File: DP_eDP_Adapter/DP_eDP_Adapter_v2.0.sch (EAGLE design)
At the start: 61 parts, among them IC1 AP6502A, IC2 tiny2313, IC3 TLC5947XLP

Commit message: 
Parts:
- SV3: value DP_EDP_ADAPTER_EDP_CONNECTOR -> DP_EDP_ADAPTER_DP_EDP_ADAPTER_EDP_CONNECTOR; device DP_eDP_Adapter:DP_EDP_ADAPTER_EDP_CONNECTOR -> DP_eDP_Adapter_v2.0:DP_EDP_ADAPTER_DP_EDP_ADAPTER_EDP_CONNECTOR
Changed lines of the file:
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@@
 <part name="+3V3" library="supply1" deviceset="+3V3" device=""/>
 <part name="SIG_OUT" library="SparkFun-Connectors" deviceset="M04" device="PTH"/>
-<part name="SV3" library="DP_eDP_Adapter" deviceset="DP_EDP_ADAPTER_EDP_CONNECTOR" device=""/>
+<part name="SV3" library="DP_eDP_Adapter_v2.0" deviceset="DP_EDP_ADAPTER_DP_EDP_ADAPTER_EDP_CONNECTOR" device=""/>
 <part name="GND4" library="supply1" deviceset="GND" device=""/>
 <part name="JP3" library="SparkFun-Connectors" deviceset="M05" device="PTH"/>

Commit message: 
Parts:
- C17: device SparkFun-Passives:CAP0402-CAP -> SparkFun-Passives:CAP0805
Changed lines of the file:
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@@
 <grid distance="0.1" unitdist="inch" unit="inch" style="lines" multiple="1" display="no" altdistance="0.01" altunitdist="inch" altunit="inch"/>
 <layers>
-<layer number="1" name="Top" color="4" fill="1" visible="no" active="no"/>
-<layer number="2" name="Route2" color="1" fill="3" visible="no" active="no"/>
-<layer number="3" name="Route3" color="4" fill="3" visible="no" active="no"/>
-<layer number="4" name="Route4" color="1" fill="4" visible="no" active="no"/>
-<layer number="5" name="Route5" color="4" fill="4" visible="no" active="no"/>
-<layer number="6" name="Route6" color="1" fill="8" visible="no" active="no"/>
-<layer number="7" name="Route7" color="4" fill="8" visible="no" active="no"/>
-<layer number="8" name="Route8" color="1" fill="2" visible="no" active="no"/>
-<layer number="9" name="Route9" color="4" fill="2" visible="no" active="no"/>
-<layer number="10" name="Route10" color="1" fill="7" visible="no" active="no"/>
-<layer number="11" name="Route11" color="4" fill="7" visible="no" active="no"/>
-<layer number="12" name="Route12" color="1" fill="5" visible="no" active="no"/>
-<layer number="13" name="Route13" color="4" fill="5" visible="no" active="no"/>
-<layer number="14" name="Route14" color="1" fill="6" visible="no" active="no"/>
-<layer number="15" name="Route15" color="4" fill="6" visible="no" active="no"/>
-<layer number="16" name="Bottom" color="1" fill="1" visible="no" active="no"/>
-<layer number="17" name="Pads" color="2" fill="1" visible="no" active="no"/>
-<layer number="18" name="Vias" color="2" fill="1" visible="no" active="no"/>
-<layer number="19" name="Unrouted" color="6" fill="1" visible="no" active="no"/>
-<layer number="20" name="Dimension" color="15" fill="1" visible="no" active="no"/>
-<layer number="21" name="tPlace" color="7" fill="1" visible="no" active="no"/>
-<layer number="22" name="bPlace" color="7" fill="1" visible="no" active="no"/>
-<layer number="23" name="tOrigins" color="15" fill="1" visible="no" active="no"/>
-<layer number="24" name="bOrigins" color="15" fill="1" visible="no" active="no"/>
-<layer number="25" name="tNames" color="7" fill="1" visible="no" active="no"/>
-<layer number="26" name="bNames" color="7" fill="1" visible="no" active="no"/>
-<layer number="27" name="tValues" color="7" fill="1" visible="no" active="no"/>
-<layer number="28" name="bValues" color="7" fill="1" visible="no" active="no"/>
+<layer number="1" name="Top" color="4" fill="1" visible="yes" active="no"/>
+<layer number="2" name="Route2" color="1" fill="3" visible="yes" active="no"/>
+<layer number="3" name="Route3" color="4" fill="3" visible="yes" active="no"/>
+<layer number="4" name="Route4" color="1" fill="4" visible="yes" active="no"/>
+<layer number="5" name="Route5" color="4" fill="4" visible="yes" active="no"/>
+<layer number="6" name="Route6" color="1" fill="8" visible="yes" active="no"/>
+<layer number="7" name="Route7" color="4" fill="8" visible="yes" active="no"/>
+<layer number="8" name="Route8" color="1" fill="2" visible="yes" active="no"/>
+<layer number="9" name="Route9" color="4" fill="2" visible="yes" active="no"/>
+<layer number="10" name="Route10" color="1" fill="7" visible="yes" active="no"/>
+<layer number="11" name="Route11" color="4" fill="7" visible="yes" active="no"/>
+<layer number="12" name="Route12" color="1" fill="5" visible="yes" active="no"/>
+<layer number="13" name="Route13" color="4" fill="5" visible="yes" active="no"/>
+<layer number="14" name="Route14" color="1" fill="6" visible="yes" active="no"/>
+<layer number="15" name="Route15" color="4" fill="6" visible="yes" active="no"/>
+<layer number="16" name="Bottom" color="1" fill="1" visible="yes" active="no"/>
+<layer number="17" name="Pads" color="2" fill="1" visible="yes" active="no"/>
+<layer number="18" name="Vias" color="2" fill="1" visible="yes" active="no"/>
+<layer number="19" name="Unrouted" color="6" fill="1" visible="yes" active="no"/>
+<layer number="20" name="Dimension" color="15" fill="1" visible="yes" active="no"/>
+<layer number="21" name="tPlace" color="7" fill="1" visible="yes" active="no"/>
+<layer number="22" name="bPlace" color="7" fill="1" visible="yes" active="no"/>
+<layer number="23" name="tOrigins" color="15" fill="1" visible="yes" active="no"/>
+<layer number="24" name="bOrigins" color="15" fill="1" visible="yes" active="no"/>
+<layer number="25" name="tNames" color="7" fill="1" visible="yes" active="no"/>
+<layer number="26" name="bNames" color="7" fill="1" visible="yes" active="no"/>
+<layer number="27" name="tValues" color="7" fill="1" visible="yes" active="no"/>
+<layer number="28" name="bValues" color="7" fill="1" visible="yes" active="no"/>
 <layer number="29" name="tStop" color="7" fill="3" visible="no" active="no"/>
 <layer number="30" name="bStop" color="7" fill="6" visible="no" active="no"/>
@@
 <layer number="35" name="tGlue" color="7" fill="4" visible="no" active="no"/>
 <layer number="36" name="bGlue" color="7" fill="5" visible="no" active="no"/>
-<layer number="37" name="tTest" color="7" fill="1" visible="no" active="no"/>
-<layer number="38" name="bTest" color="7" fill="1" visible="no" active="no"/>
+<layer number="37" name="tTest" color="7" fill="1" visible="yes" active="no"/>
+<layer number="38" name="bTest" color="7" fill="1" visible="yes" active="no"/>
 <layer number="39" name="tKeepout" color="4" fill="11" visible="no" active="no"/>
 <layer number="40" name="bKeepout" color="1" fill="11" visible="no" active="no"/>
@@
 <layer number="44" name="Drills" color="7" fill="1" visible="no" active="no"/>
 <layer number="45" name="Holes" color="7" fill="1" visible="no" active="no"/>
-<layer number="46" name="Milling" color="3" fill="1" visible="no" active="no"/>
-<layer number="47" name="Measures" color="7" fill="1" visible="no" active="no"/>
-<layer number="48" name="Document" color="7" fill="1" visible="no" active="no"/>
-<layer number="49" name="Reference" color="7" fill="1" visible="no" active="no"/>
-<layer number="50" name="dxf" color="7" fill="1" visible="no" active="no"/>
-<layer number="51" name="tDocu" color="7" fill="1" visible="no" active="no"/>
-<layer number="52" name="bDocu" color="7" fill="1" visible="no" active="no"/>
-<layer number="53" name="tGND_GNDA" color="7" fill="1" visible="no" active="no"/>
-<layer number="54" name="bGND_GNDA" color="7" fill="1" visible="no" active="no"/>
-<layer number="56" name="wert" color="7" fill="1" visible="no" active="no"/>
+<layer number="46" name="Milling" color="3" fill="1" visible="yes" active="no"/>
+<layer number="47" name="Measures" color="7" fill="1" visible="yes" active="no"/>
+<layer number="48" name="Document" color="7" fill="1" visible="yes" active="no"/>
+<layer number="49" name="Reference" color="7" fill="1" visible="yes" active="no"/>
+<layer number="50" name="dxf" color="7" fill="1" visible="yes" active="no"/>
+<layer number="51" name="tDocu" color="7" fill="1" visible="yes" active="no"/>
+<layer number="52" name="bDocu" color="7" fill="1" visible="yes" active="no"/>
+<layer number="53" name="tGND_GNDA" color="7" fill="1" visible="yes" active="no"/>
+<layer number="54" name="bGND_GNDA" color="7" fill="1" visible="yes" active="no"/>
+<layer number="56" name="wert" color="7" fill="1" visible="yes" active="no"/>
 <layer number="91" name="Nets" color="2" fill="1" visible="yes" active="yes"/>
 <layer number="92" name="Busses" color="1" fill="1" visible="yes" active="yes"/>
@@
 <part name="R5" library="SparkFun-Passives" deviceset="RESISTOR" device="0402-RES" value="26.1K"/>
 <part name="C15" library="SparkFun-Passives" deviceset="CAP" device="1206" value="10nF"/>
-<part name="C17" library="SparkFun-Passives" deviceset="CAP" device="0402-CAP" value="22Uf"/>
+<part name="C17" library="SparkFun-Passives" deviceset="CAP" device="0805" value="22Uf"/>
 <part name="JP4" library="SparkFun-Connectors" deviceset="M05" device="PTH"/>
 <part name="GND15" library="supply1" deviceset="GND" device=""/>

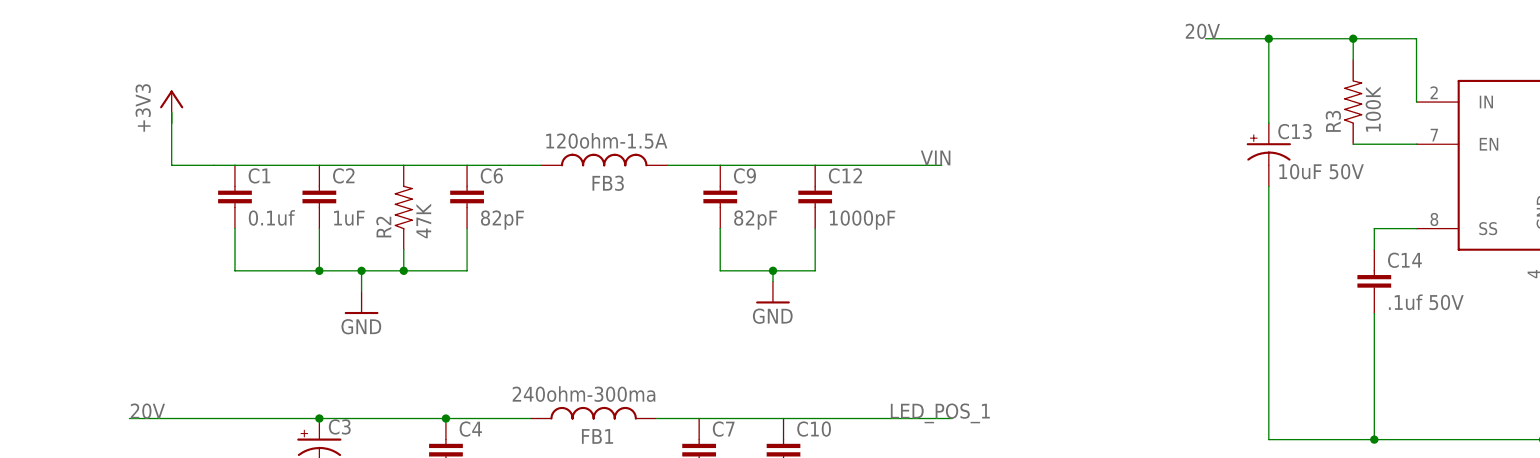
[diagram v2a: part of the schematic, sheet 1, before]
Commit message: 
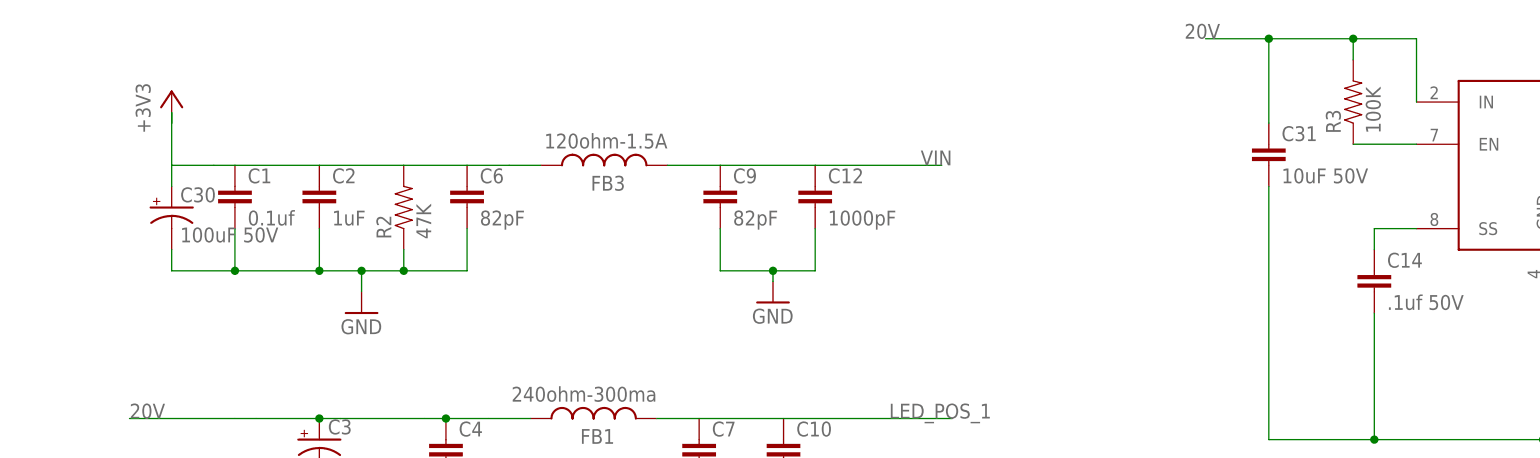
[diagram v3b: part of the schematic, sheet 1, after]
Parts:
- removed C13: 10uF 50V, SparkFun-Passives:CAP_POL6032
- added C30: 100uF 50V, SparkFun-Passives:CAP_POL6032
- added C31: 10uF 50V, SparkFun-Passives:CAP1206
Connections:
- net +3V3: now also C30.+
- net 20V: now also C31.1; no longer C13.+
- net GND: now also C30.-, C31.2; no longer C13.-
